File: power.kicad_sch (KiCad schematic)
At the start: 7 parts, among them IC1 AP63203WU-7, J1 Barrel_Jack_Switch_Pin3Ring

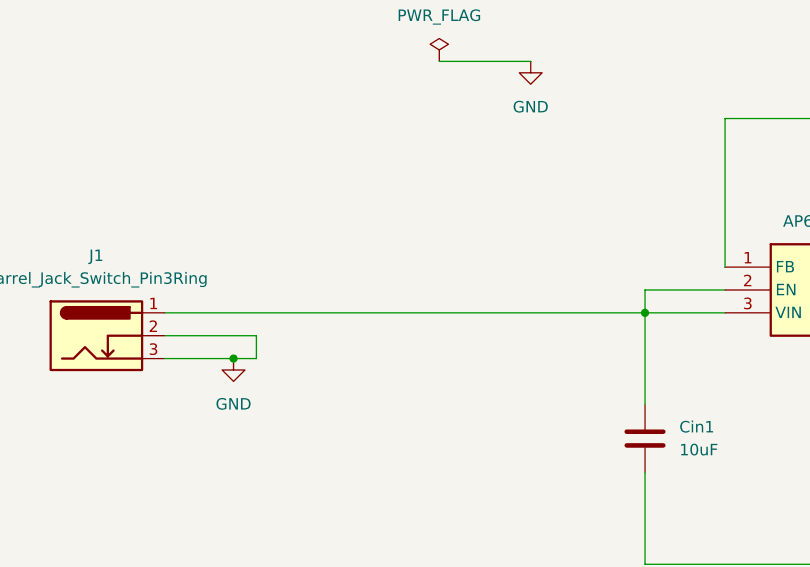
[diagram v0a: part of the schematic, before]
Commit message: fix: add schottky diode on main alim
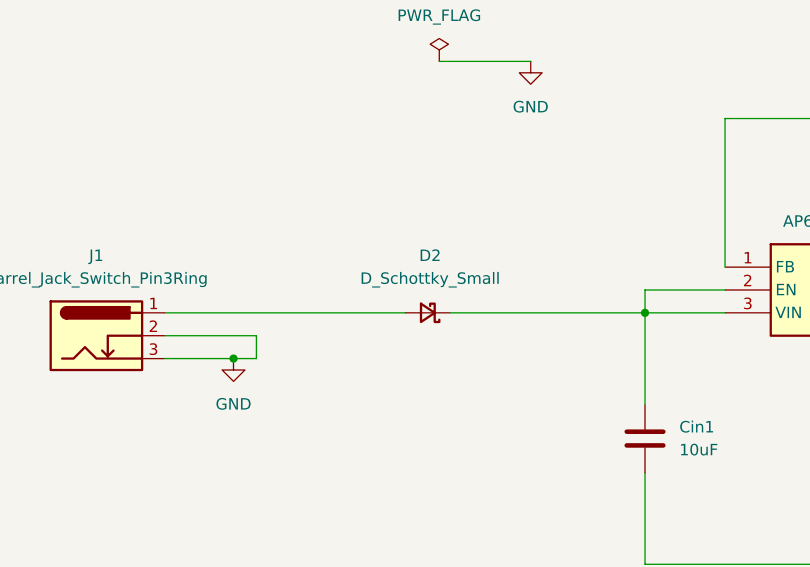
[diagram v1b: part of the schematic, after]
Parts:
- added D2: D_Schottky_Small, symbol Device:D_Schottky_Small
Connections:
- net at Cin1.2, IC1.2 (EN), IC1.3 (VIN): now also D2.1 (K); no longer J1.1
- new net: D2.2 (A), J1.1
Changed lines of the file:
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@@
+	(wire
+		(pts
+			(xy 78.74 68.58) (xy 105.41 68.58)
+		)
+		(stroke
+			(width 0)
+			(type default)
+		)
+	)
 	(wire
 		(pts
@@
 	(wire
 		(pts
-			(xy 78.74 68.58) (xy 132.08 68.58)
-		)
-		(stroke
-			(width 0)
-			(type default)
-		)
-	)
-	(wire
-		(pts
 			(xy 218.44 66.04) (xy 218.44 77.47)
 		)
@@
 		(pts
 			(xy 140.97 63.5) (xy 140.97 46.99)
+		)
+		(stroke
+			(width 0)
+			(type default)
+		)
+	)
+	(wire
+		(pts
+			(xy 110.49 68.58) (xy 132.08 68.58)
 		)
 		(stroke
@@
 					(unit 1)
 				)
+			)
+		)
+	)
+	(symbol
+		(lib_id "Device:D_Schottky_Small")
+		(at 107.95 68.58 180)
+		(unit 1)
+		(exclude_from_sim no)
+		(in_bom yes)
+		(on_board yes)
+		(dnp no)
+		(fields_autoplaced yes)
+		(property "Reference" "D2"
+			(at 108.204 62.23 0)
+			(effects
+				(font
+					(size 1.27 1.27)
+				)
+			)
+		)
+		(property "Value" "D_Schottky_Small"
+			(at 108.204 64.77 0)
+			(effects
+				(font
+					(size 1.27 1.27)
+				)
+			)
+		)
+		(property "Footprint" ""
+			(at 107.95 68.58 90)
+			(effects
+				(font
+					(size 1.27 1.27)
+				)
+				(hide yes)
+			)
+		)
+		(property "Datasheet" "~"
+			(at 107.95 68.58 90)
+			(effects
+				(font
+					(size 1.27 1.27)
+				)
+				(hide yes)
+			)
+		)
+		(property "Description" "Schottky diode, small symbol"
+			(at 107.95 68.58 0)
+			(effects
+				(font
+					(size 1.27 1.27)
+				)
+				(hide yes)
+			)
+		)
+		(pin "2"
+		)
+		(pin "1"
+		)
+		(instances
+			(project ""
+				(path "/08ef31dc-81c2-4bcd-8336-e62c344e451e/760387e1-ffe6-428e-8651-2617e5a76fa2"
+					(reference "D2")
+					(unit 1)
+				)

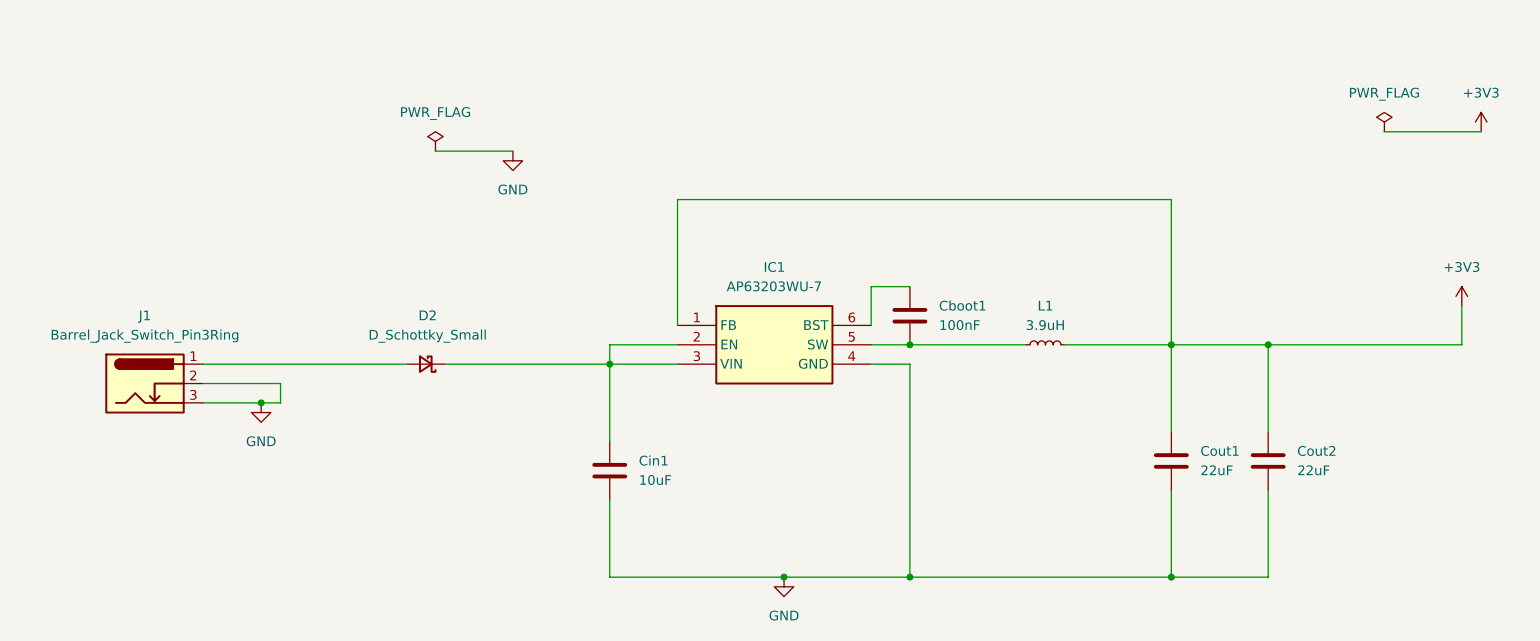
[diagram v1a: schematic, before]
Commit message: feat: add +5V power symbol for uart programming
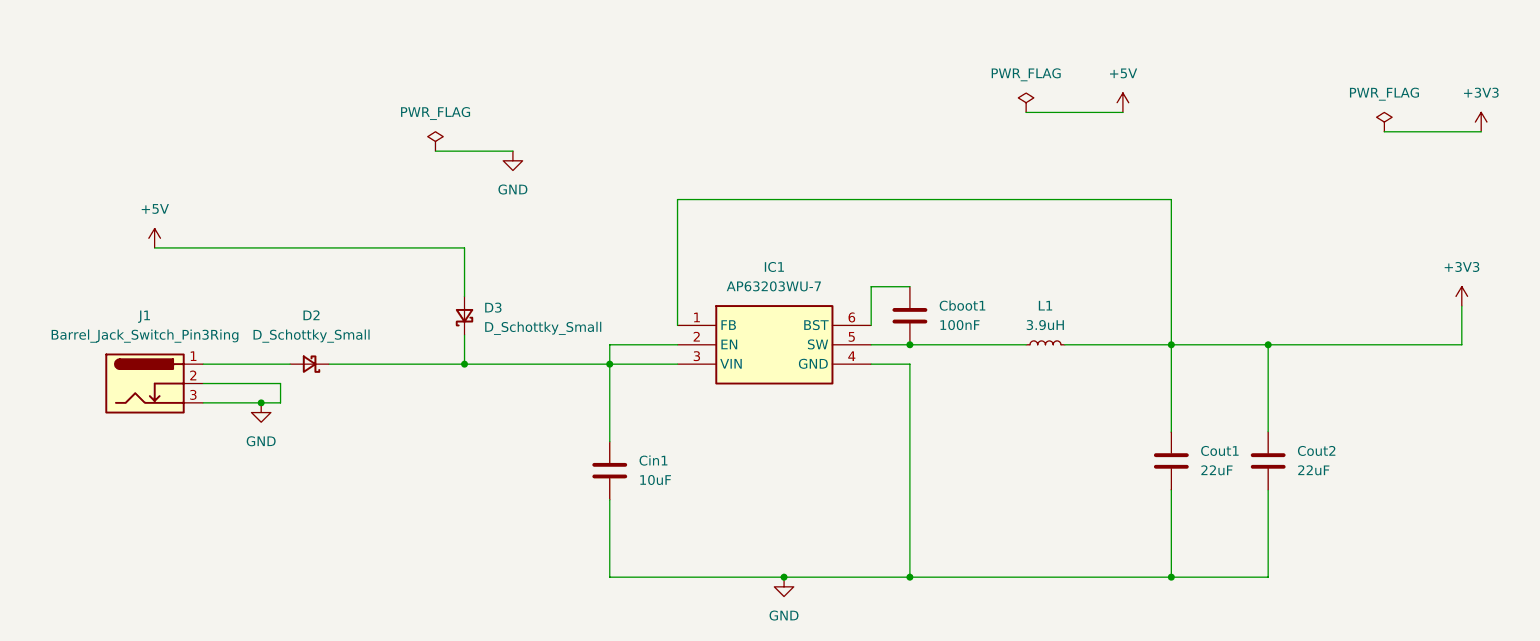
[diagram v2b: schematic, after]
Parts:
- added D3: D_Schottky_Small, symbol Device:D_Schottky_Small
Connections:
- net at Cin1.2, D2.1 (K), IC1.2 (EN)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: now also D3.1 (K)
- new net +5V: D3.2 (A)
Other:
- moved on the sheet: D2

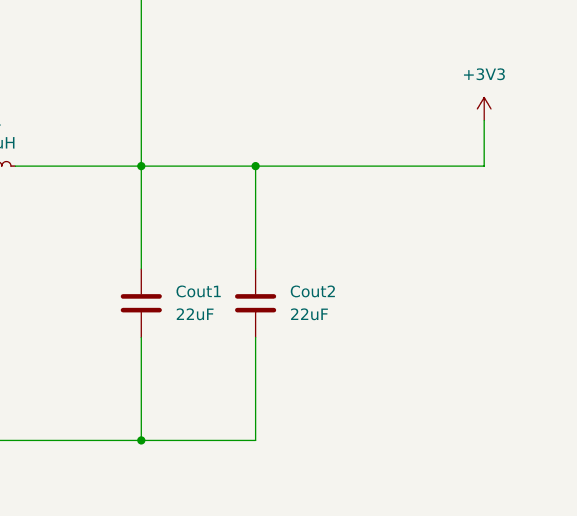
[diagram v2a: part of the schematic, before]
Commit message: feat: add led at buck converter out pin
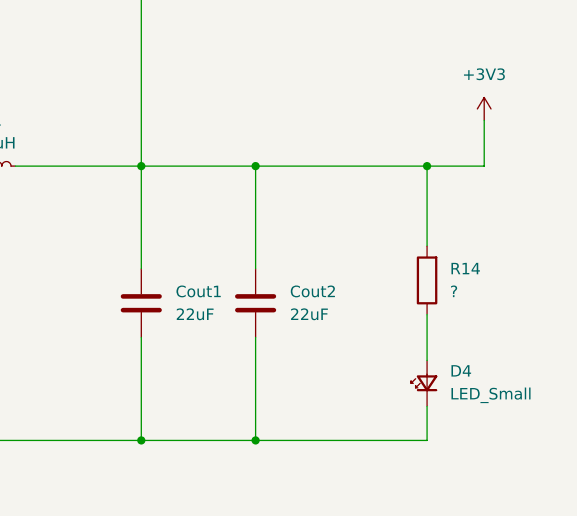
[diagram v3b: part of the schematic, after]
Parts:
- added D4: LED_Small, LED_SMD:LED_0805_2012Metric, symbol Device:LED_Small
- added R14: ?, Resistor_THT:R_Axial_DIN0207_L6.3mm_D2.5mm_P7.62mm_Horizontal, symbol Device:R
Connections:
- net +3V3: now also R14.2
- net GND: now also D4.1 (K)
- new net: D4.2 (A), R14.1
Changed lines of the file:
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@@
 	(paper "A4")
+	(junction
+		(at 237.49 66.04)
+		(diameter 0)
+		(color 0 0 0 0)
+	)
 	(junction
 		(at 86.36 73.66)
@@
 	)
 	(junction
+		(at 218.44 96.52)
+		(diameter 0)
+		(color 0 0 0 0)
+	)
+	(junction
 		(at 132.08 68.58)
 		(diameter 0)
@@
 	(wire
 		(pts
+			(xy 237.49 92.71) (xy 237.49 96.52)
+		)
+		(stroke
+			(width 0)
+			(type default)
+		)
+	)
+	(wire
+		(pts
+			(xy 237.49 82.55) (xy 237.49 87.63)
+		)
+		(stroke
+			(width 0)
+			(type default)
+		)
+	)
+	(wire
+		(pts
 			(xy 166.37 66.04) (xy 171.45 66.04)
 		)
@@
 	(wire
 		(pts
-			(xy 218.44 66.04) (xy 243.84 66.04)
+			(xy 218.44 66.04) (xy 237.49 66.04)
 		)
 		(stroke
@@
 	(wire
 		(pts
+			(xy 237.49 66.04) (xy 243.84 66.04)
+		)
+		(stroke
+			(width 0)
+			(type default)
+		)
+	)
+	(wire
+		(pts
+			(xy 218.44 96.52) (xy 237.49 96.52)
+		)
+		(stroke
+			(width 0)
+			(type default)
+		)
+	)
+	(wire
+		(pts
 			(xy 218.44 66.04) (xy 218.44 77.47)
 		)
@@
 		(pts
 			(xy 88.9 71.12) (xy 88.9 73.66)
+		)
+		(stroke
+			(width 0)
+			(type default)
+		)
+	)
+	(wire
+		(pts
+			(xy 237.49 66.04) (xy 237.49 74.93)
 		)
 		(stroke
@@
 					(unit 1)
 				)
+			)
+		)
+	)
+	(symbol
+		(lib_id "Device:R")
+		(at 237.49 78.74 180)
+		(unit 1)
+		(exclude_from_sim no)
+		(in_bom yes)
+		(on_board yes)
+		(dnp no)
+		(fields_autoplaced yes)
+		(property "Reference" "R14"
+			(at 240.03 77.47 0)
+			(effects
+				(font
+					(size 1.27 1.27)
+				)
+				(justify right)
+			)
+		)
+		(property "Value" "?"
+			(at 240.03 80.01 0)
+			(effects
+				(font
+					(size 1.27 1.27)
+				)
+				(justify right)
+			)
+		)
+		(property "Footprint" "Resistor_THT:R_Axial_DIN0207_L6.3mm_D2.5mm_P7.62mm_Horizontal"
+			(at 239.268 78.74 90)
+			(effects
+				(font
+					(size 1.27 1.27)
+				)
+				(hide yes)
+			)
+		)
+		(property "Datasheet" "ok"
+			(at 237.49 78.74 0)
+			(effects
+				(font
+					(size 1.27 1.27)
+				)
+				(hide yes)
+			)
+		)
+		(property "Description" ""
+			(at 237.49 78.74 0)
+			(effects
+				(font
+					(size 1.27 1.27)
+				)
+				(hide yes)
+			)
+		)
+		(pin "2"
+		)
+		(pin "1"
+		)
+		(instances
+			(project "pv_router"
+				(path "/08ef31dc-81c2-4bcd-8336-e62c344e451e/760387e1-ffe6-428e-8651-2617e5a76fa2"
+					(reference "R14")
+					(unit 1)
+				)
+			)
+		)
+	)
+	(symbol
+		(lib_id "Device:LED_Small")
+		(at 237.49 90.17 90)
+		(unit 1)
+		(exclude_from_sim no)
+		(in_bom yes)
+		(on_board yes)
+		(dnp no)
+		(fields_autoplaced yes)
+		(property "Reference" "D4"
+			(at 240.03 88.8365 90)
+			(effects
+				(font
+					(size 1.27 1.27)
+				)
+				(justify right)
+			)
+		)
+		(property "Value" "LED_Small"
+			(at 240.03 91.3765 90)
+			(effects
+				(font
+					(size 1.27 1.27)
+				)
+				(justify right)
+			)
+		)
+		(property "Footprint" "LED_SMD:LED_0805_2012Metric"
+			(at 237.49 90.17 90)
+			(effects
+				(font
+					(size 1.27 1.27)
+				)
+				(hide yes)
+			)
+		)
+		(property "Datasheet" "~"
+			(at 237.49 90.17 90)
+			(effects
+				(font
+					(size 1.27 1.27)
+				)
+				(hide yes)
+			)
+		)
+		(property "Description" ""
+			(at 237.49 90.17 0)
+			(effects
+				(font
+					(size 1.27 1.27)
+				)
+				(hide yes)
+			)
+		)
+		(pin "2"
+		)
+		(pin "1"
+		)
+		(instances
+			(project "pv_router"
+				(path "/08ef31dc-81c2-4bcd-8336-e62c344e451e/760387e1-ffe6-428e-8651-2617e5a76fa2"
+					(reference "D4")
+					(unit 1)
+				)

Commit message: fix: change 1k resistor array to 2 resistors
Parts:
- D2, D3: footprint (none) -> Diode_THT:D_T-1_P10.16mm_Horizontal
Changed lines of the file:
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@@
 			)
 		)
-		(property "Footprint" ""
+		(property "Footprint" "Diode_THT:D_T-1_P10.16mm_Horizontal"
 			(at 113.03 62.23 90)
 			(effects
@@
 			)
 		)
-		(property "Footprint" ""
+		(property "Footprint" "Diode_THT:D_T-1_P10.16mm_Horizontal"
 			(at 92.71 68.58 90)
 			(effects

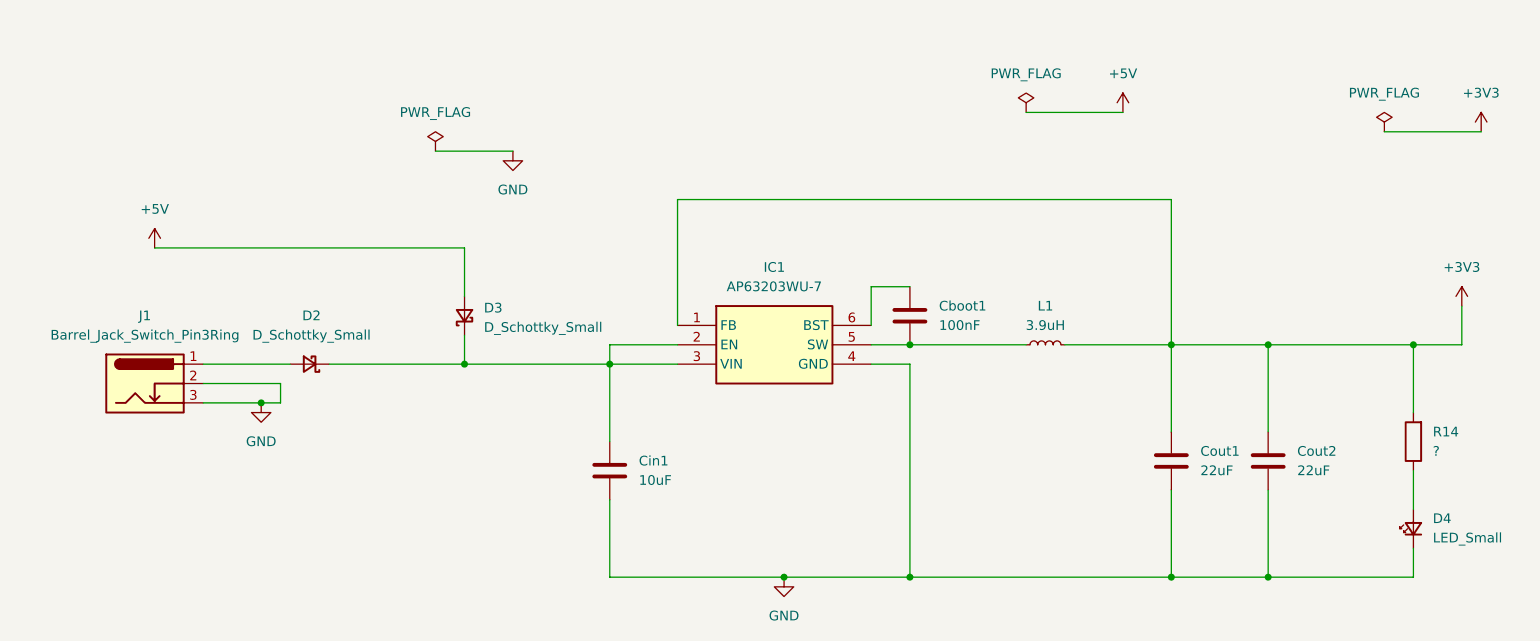
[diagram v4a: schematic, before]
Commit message: fix: add connector JST to SSR device
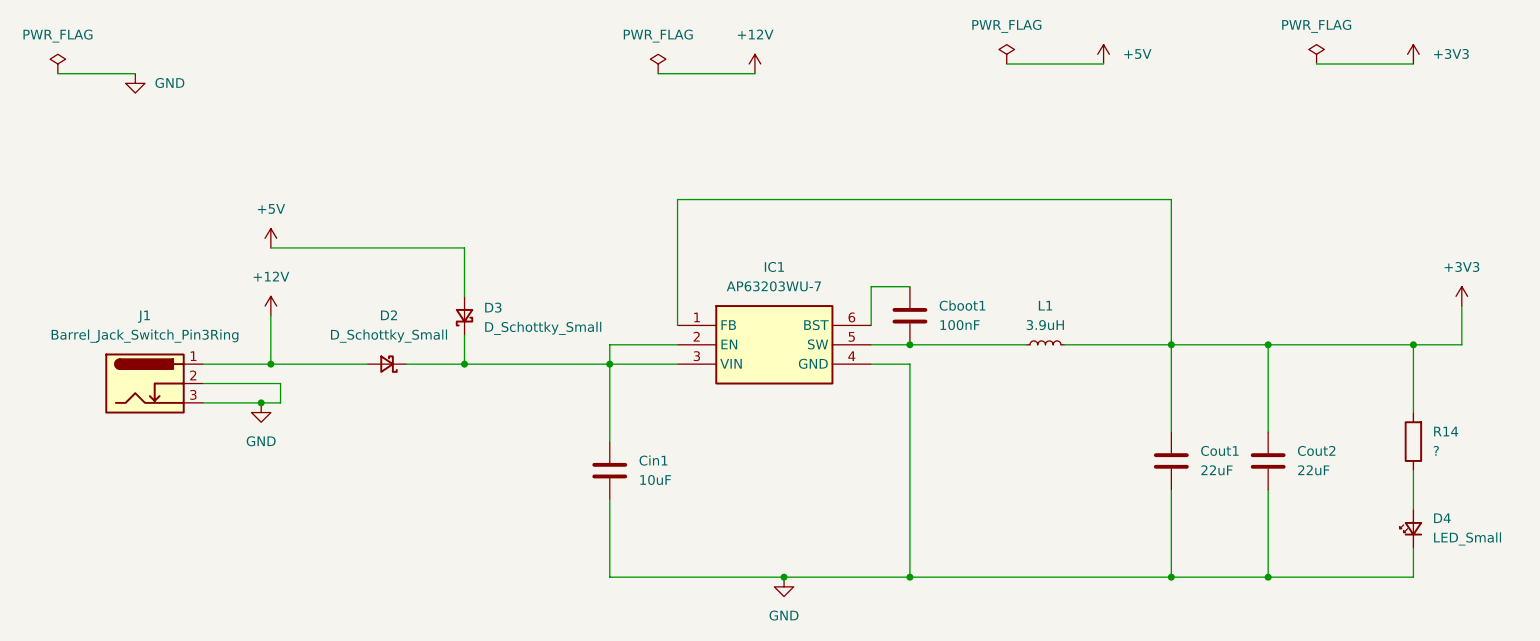
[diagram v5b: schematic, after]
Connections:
- net +12V: now reaches D2.2 (A), J1.1
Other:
- moved on the sheet: D2

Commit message: fix: after ERC check
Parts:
- IC1: footprint KiCad:AP63203WU7 -> AP63203WU7
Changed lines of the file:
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@@
 			)
 		)
-		(property "Datasheet" "ok 2 !!FP"
+		(property "Datasheet" "~"
 			(at 72.39 72.136 0)
 			(effects
@@
 			)
 		)
-		(property "Description" ""
+		(property "Description" "DC Barrel Jack with an internal switch"
 			(at 71.12 71.12 0)
 			(effects
@@
 			)
 		)
-		(property "Description" ""
+		(property "Description" "Power symbol creates a global label with name \"GND\" , ground"
 			(at 86.36 73.66 0)
 			(effects
@@
 			)
 		)
-		(property "Datasheet" "1 ok"
+		(property "Datasheet" "~"
 			(at 205.74 81.28 0)
 			(effects
@@
 			)
 		)
-		(property "Description" ""
+		(property "Description" "Unpolarized capacitor"
 			(at 205.74 81.28 0)
 			(effects
@@
 			)
 		)
-		(property "Footprint" "KiCad:AP63203WU7"
+		(property "Footprint" "AP63203WU7"
 			(at 162.56 158.42 0)
 			(effects
@@
 			)
 		)
-		(property "Description" ""
+		(property "Description" "Special symbol for telling ERC where power comes from"
 			(at 138.43 30.48 0)
 			(effects
@@
 			)
 		)
-		(property "Description" ""
+		(property "Description" "Power symbol creates a global label with name \"GND\" , ground"
 			(at 154.94 96.52 0)
 			(effects
@@
 			)
 		)
-		(property "Description" ""
+		(property "Description" "Special symbol for telling ERC where power comes from"
 			(at 184.15 29.21 0)
 			(effects
@@
 			)
 		)
-		(property "Datasheet" "ok"
+		(property "Datasheet" "~"
 			(at 237.49 78.74 0)
 			(effects
@@
 			)
 		)
-		(property "Description" ""
+		(property "Description" "Resistor"
 			(at 237.49 78.74 0)
 			(effects
@@
 			)
 		)
-		(property "Description" ""
+		(property "Description" "Light emitting diode, small symbol"
+			(at 237.49 90.17 0)
+			(effects
+				(font
+					(size 1.27 1.27)
+				)
+				(hide yes)
+			)
+		)
+		(property "Sim.Pin" "1=K 2=A"
 			(at 237.49 90.17 0)
 			(effects
@@
 			)
 		)
-		(property "Description" ""
+		(property "Description" "Special symbol for telling ERC where power comes from"
 			(at 224.79 29.21 0)
 			(effects
@@
 			)
 		)
-		(property "Description" ""
+		(property "Description" "Power symbol creates a global label with name \"GND\" , ground"
 			(at 69.85 30.48 0)
 			(effects
@@
 			)
 		)
-		(property "Datasheet" "1 ok"
+		(property "Datasheet" "~"
 			(at 132.08 82.55 0)
 			(effects
@@
 			)
 		)
-		(property "Description" ""
+		(property "Description" "Unpolarized capacitor"
 			(at 132.08 82.55 0)
 			(effects
@@
 			)
 		)
-		(property "Description" ""
+		(property "Description" "Power symbol creates a global label with name \"+3V3\""
 			(at 243.84 60.96 0)
 			(effects
@@
 			)
 		)
-		(property "Description" ""
+		(property "Description" "Power symbol creates a global label with name \"+3V3\""
 			(at 237.49 29.21 0)
 			(effects
@@
 			)
 		)
-		(property "Description" ""
+		(property "Description" "Special symbol for telling ERC where power comes from"
 			(at 59.69 30.48 0)
 			(effects
@@
 			)
 		)
-		(property "Datasheet" "ok: 1"
+		(property "Datasheet" "~"
 			(at 171.45 62.23 0)
 			(effects
@@
 			)
 		)
-		(property "Description" ""
+		(property "Description" "Unpolarized capacitor"
 			(at 171.45 62.23 0)
 			(effects
@@
 			)
 		)
-		(property "Datasheet" "1 ok"
+		(property "Datasheet" "~"
 			(at 218.44 81.28 0)
 			(effects
@@
 			)
 		)
-		(property "Description" ""
+		(property "Description" "Unpolarized capacitor"
 			(at 218.44 81.28 0)
 			(effects
@@
 			)
 		)
-		(property "Datasheet" "1 ok"
+		(property "Datasheet" "~"
 			(at 189.23 66.04 0)
 			(effects
@@
 			)
 		)
-		(property "Description" ""
+		(property "Description" "Inductor, small symbol"
 			(at 189.23 66.04 0)
 			(effects

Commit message: fix: fix components footprints, resistors, crystal
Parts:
- IC1: footprint AP63203WU7 -> Buck_conv:AP63203WU7
- L1: footprint MSS1038T-333MLC:MSS1038T333MLC -> Inductor_SMD:L_Bourns-SRN6028
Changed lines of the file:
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@@
 			)
 		)
-		(property "Footprint" "AP63203WU7"
+		(property "Footprint" "Buck_conv:AP63203WU7"
 			(at 162.56 158.42 0)
 			(effects
@@
 			)
 		)
-		(property "Footprint" "MSS1038T-333MLC:MSS1038T333MLC"
+		(property "Footprint" "Inductor_SMD:L_Bourns-SRN6028"
 			(at 189.23 66.04 0)
 			(effects
